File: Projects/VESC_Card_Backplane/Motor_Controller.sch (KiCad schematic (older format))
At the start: 0 parts

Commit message: Added stuff to VESC_Card_Backplane
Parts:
- added P?: AMP17614426-2_EDGE, symbol AMP17614426-2_EDGE
- added P?: EC90_Flat, symbol EC90_Flat
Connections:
- new net W: P?.1 (W), P?.7 (P7)
- no-connect marks 0 -> 1
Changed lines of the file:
@@
 $Descr A4 11693 8268
 encoding utf-8
-Sheet 1 5
+Sheet 3 5
 Title ""
 Date ""
@@
 Comment4 ""
 $EndDescr
+$Comp
+L AMP17614426-2_EDGE P?
+U 1 1 5871B697
+P 5025 3325
+F 0 "P?" H 5025 3775 60  0000 C CNN
+F 1 "AMP17614426-2_EDGE" H 5075 1875 60  0000 C CNN
+F 2 "" H 5175 3325 60  0000 C CNN
+F 3 "" H 5175 3325 60  0000 C CNN
+	1    5025 3325
+	1    0    0    -1
+$EndComp
+NoConn ~ 4525 4575
+$Comp
+L EC90_Flat P?
+U 1 1 5871BA09
+P 3325 4325
+F 0 "P?" H 3325 4575 50  0000 C CNN
+F 1 "EC90_Flat" H 3325 4075 50  0000 C CNN
+F 2 "" H 3325 3125 50  0000 C CNN
+F 3 "" H 3325 3125 50  0000 C CNN
+	1    3325 4325
+	1    0    0    -1
+$EndComp
+Text Label 4525 3075 0    60   ~ 0
+W
+Text Label 3575 4375 0    60   ~ 0
+W
 $EndSCHEMATC

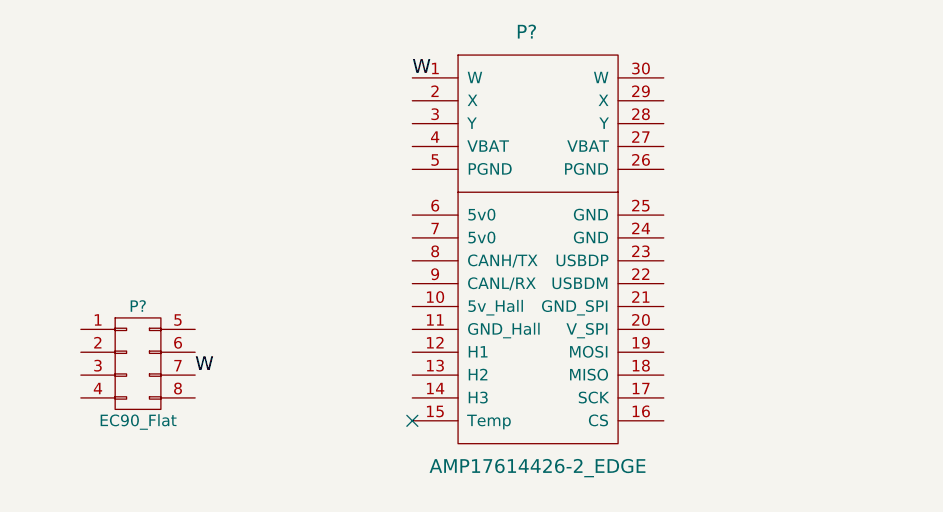
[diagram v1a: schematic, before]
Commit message: Partially did motorcontroller part of schematic
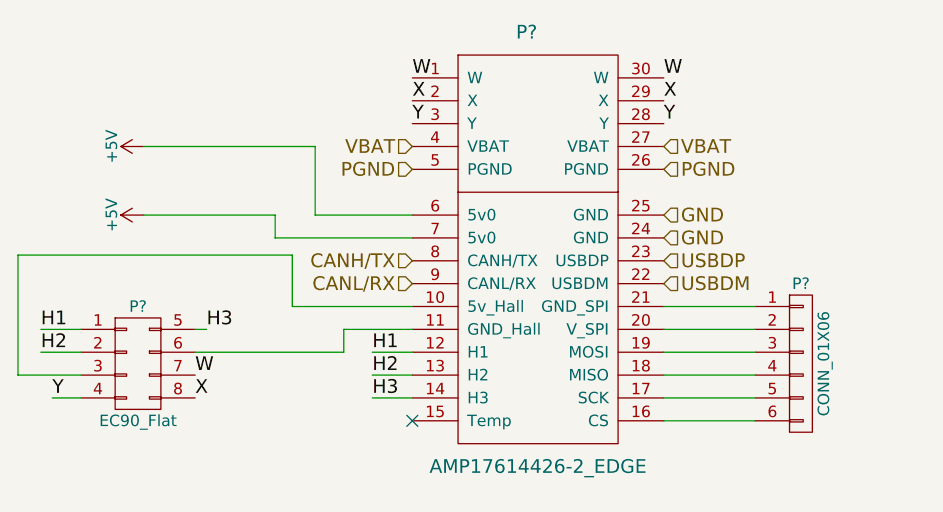
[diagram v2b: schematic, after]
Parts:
- added P?: CONN_01X06, symbol CONN_01X06
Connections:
- net W: now also P?.30 (W)
- net at P?.10 (5v_Hall): now also P?.3 (P3)
- net at P?.11 (GND_Hall): now also P?.6 (P6)
- net H1: now reaches P?.12 (H1)
- net H1: now also P?.1 (P1)
- net H2: now reaches P?.13 (H2)
- net H2: now also P?.2 (P2)
- net H3: now reaches P?.14 (H3)
- net H3: now also P?.5 (P5)
- net at P?.16 (CS): now also P?.6 (P6)
- net at P?.17 (SCK): now also P?.5 (P5)
- net at P?.18 (MISO): now also P?.4 (P4)
- net at P?.19 (MOSI): now also P?.3 (P3)
- net X: now reaches P?.2 (X)
- net X: now also P?.29 (X), P?.8 (P8)
- net at P?.20 (V_SPI): now also P?.2 (P2)
- net at P?.21 (GND_SPI): now also P?.1 (P1)
- net USBDM: now reaches P?.22 (USBDM)
- net USBDP: now reaches P?.23 (USBDP)
- net GND: now reaches P?.24 (GND)
- net GND: now also P?.25 (GND)
- net PGND: now reaches P?.26 (PGND)
- net PGND: now also P?.5 (PGND)
- net VBAT: now reaches P?.27 (VBAT)
- net VBAT: now also P?.4 (VBAT)
- net Y: now reaches P?.28 (Y)
- net Y: now also P?.3 (Y), P?.4 (P4)
- net +5V: now reaches P?.6 (5v0)
- net +5V: now also P?.7 (5v0)
- net CANH/TX: now reaches P?.8 (CANH/TX)
- net CANL/RX: now reaches P?.9 (CANL/RX)
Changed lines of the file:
@@
 Text Label 3575 4375 0    60   ~ 0
 W
+Text Label 3575 4475 0    60   ~ 0
+X
+Text Label 4525 3175 0    60   ~ 0
+X
+Text Label 4525 3275 0    60   ~ 0
+Y
+Text Label 2950 4475 0    60   ~ 0
+Y
+Text Label 4350 4275 0    60   ~ 0
+H1
+Text Label 4350 4375 0    60   ~ 0
+H2
+Text Label 4350 4475 0    60   ~ 0
+H3
+Text Label 2900 4175 0    60   ~ 0
+H1
+Text Label 2900 4275 0    60   ~ 0
+H2
+Text Label 3625 4175 0    60   ~ 0
+H3
+Text HLabel 4525 3375 0    60   Input ~ 0
+VBAT
+Text HLabel 4525 3475 0    60   Input ~ 0
+PGND
+$Comp
+L +5V #PWR?
+U 1 1 5871CFED
+P 3350 3375
+F 0 "#PWR?" H 3350 3225 50  0001 C CNN
+F 1 "+5V" H 3350 3515 50  0000 C CNN
+F 2 "" H 3350 3375 50  0000 C CNN
+F 3 "" H 3350 3375 50  0000 C CNN
+	1    3350 3375
+	0    -1   -1   0
+$EndComp
+$Comp
+L +5V #PWR?
+U 1 1 5871D005
+P 3350 3675
+F 0 "#PWR?" H 3350 3525 50  0001 C CNN
+F 1 "+5V" H 3350 3815 50  0000 C CNN
+F 2 "" H 3350 3675 50  0000 C CNN
+F 3 "" H 3350 3675 50  0000 C CNN
+	1    3350 3675
+	0    -1   -1   0
+$EndComp
+Text HLabel 4525 3875 0    60   Input ~ 0
+CANH/TX
+Text HLabel 4525 3975 0    60   Input ~ 0
+CANL/RX
+Wire Wire Line
+	4525 4275 4350 4275
+Wire Wire Line
+	4525 4375 4350 4375
+Wire Wire Line
+	4525 4475 4350 4475
+Wire Wire Line
+	3575 4275 4225 4275
+Wire Wire Line
+	4225 4275 4225 4175
+Wire Wire Line
+	4225 4175 4525 4175
+Wire Wire Line
+	3075 4375 2800 4375
+Wire Wire Line
+	2800 4375 2800 3850
+Wire Wire Line
+	2800 3850 4000 3850
+Wire Wire Line
+	4000 3850 4000 4075
+Wire Wire Line
+	4000 4075 4525 4075
+Wire Wire Line
+	2900 4175 3075 4175
+Wire Wire Line
+	2900 4275 3075 4275
+Wire Wire Line
+	2950 4475 3075 4475
+Wire Wire Line
+	3625 4175 3575 4175
+Wire Wire Line
+	3350 3375 4100 3375
+Wire Wire Line
+	3350 3675 3925 3675
+Wire Wire Line
+	3925 3675 3925 3775
+Wire Wire Line
+	3925 3775 4525 3775
+Wire Wire Line
+	4100 3375 4100 3675
+Wire Wire Line
+	4100 3675 4525 3675
+Text HLabel 5625 3875 2    60   Input ~ 0
+USBDP
+Text HLabel 5625 3975 2    60   Input ~ 0
+USBDM
+Text Label 5625 3075 0    60   ~ 0
+W
+Text Label 5625 3175 0    60   ~ 0
+X
+Text Label 5625 3275 0    60   ~ 0
+Y
+Text HLabel 5625 3375 2    60   Input ~ 0
+VBAT
+Text HLabel 5625 3475 2    60   Input ~ 0
+PGND
+Text HLabel 5625 3675 2    60   Input ~ 0
+GND
+Text HLabel 5625 3775 2    60   Input ~ 0
+GND
+$Comp
+L CONN_01X06 P?
+U 1 1 5871D4B0
+P 6225 4325
+F 0 "P?" H 6225 4675 50  0000 C CNN
+F 1 "CONN_01X06" V 6325 4325 50  0000 C CNN
+F 2 "" H 6225 4325 50  0000 C CNN
+F 3 "" H 6225 4325 50  0000 C CNN
+	1    6225 4325
+	1    0    0    -1
+$EndComp
+Wire Wire Line
+	6025 4075 5625 4075
+Wire Wire Line
+	5625 4175 6025 4175
+Wire Wire Line
+	6025 4275 5625 4275
+Wire Wire Line
+	5625 4375 6025 4375
+Wire Wire Line
+	6025 4475 5625 4475
+Wire Wire Line
+	5625 4575 6025 4575
 $EndSCHEMATC

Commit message: Updated subsheets and added CAN bus :)
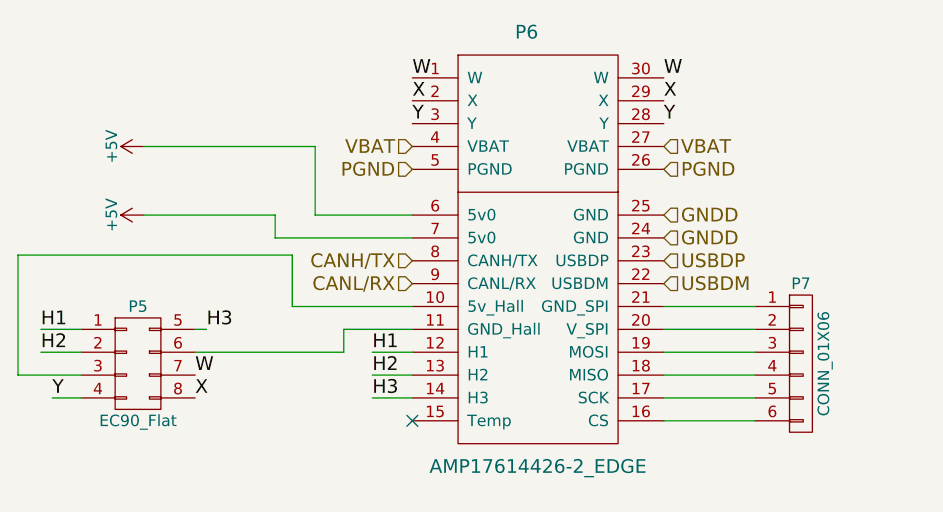
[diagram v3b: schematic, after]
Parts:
- gave numbers to parts that had none: 3
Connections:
- net GND renamed GNDD
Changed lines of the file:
@@
 $Descr A4 11693 8268
 encoding utf-8
-Sheet 3 5
+Sheet 6 6
 Title ""
 Date ""
@@
 $EndDescr
 $Comp
-L AMP17614426-2_EDGE P?
+L AMP17614426-2_EDGE P2
 U 1 1 5871B697
 P 5025 3325
-F 0 "P?" H 5025 3775 60  0000 C CNN
+AR Path="/5871DA4F/5871B697" Ref="P2"  Part="1"
+AR Path="/5878CF59/5871B697" Ref="P6"  Part="1"
+F 0 "P6" H 5025 3775 60  0000 C CNN
 F 1 "AMP17614426-2_EDGE" H 5075 1875 60  0000 C CNN
 F 2 "" H 5175 3325 60  0000 C CNN
@@
 NoConn ~ 4525 4575
 $Comp
-L EC90_Flat P?
+L EC90_Flat P1
 U 1 1 5871BA09
 P 3325 4325
-F 0 "P?" H 3325 4575 50  0000 C CNN
+AR Path="/5871DA4F/5871BA09" Ref="P1"  Part="1"
+AR Path="/5878CF59/5871BA09" Ref="P5"  Part="1"
+F 0 "P5" H 3325 4575 50  0000 C CNN
 F 1 "EC90_Flat" H 3325 4075 50  0000 C CNN
 F 2 "" H 3325 3125 50  0000 C CNN
@@
 PGND
 $Comp
-L +5V #PWR?
+L +5V #PWR4
 U 1 1 5871CFED
 P 3350 3375
-F 0 "#PWR?" H 3350 3225 50  0001 C CNN
+AR Path="/5871DA4F/5871CFED" Ref="#PWR4"  Part="1"
+AR Path="/5878CF59/5871CFED" Ref="#PWR10"  Part="1"
+F 0 "#PWR10" H 3350 3225 50  0001 C CNN
 F 1 "+5V" H 3350 3515 50  0000 C CNN
 F 2 "" H 3350 3375 50  0000 C CNN
@@
 $EndComp
 $Comp
-L +5V #PWR?
+L +5V #PWR5
 U 1 1 5871D005
 P 3350 3675
-F 0 "#PWR?" H 3350 3525 50  0001 C CNN
+AR Path="/5871DA4F/5871D005" Ref="#PWR5"  Part="1"
+AR Path="/5878CF59/5871D005" Ref="#PWR11"  Part="1"
+F 0 "#PWR11" H 3350 3525 50  0001 C CNN
 F 1 "+5V" H 3350 3815 50  0000 C CNN
 F 2 "" H 3350 3675 50  0000 C CNN
@@
 PGND
 Text HLabel 5625 3675 2    60   Input ~ 0
-GND
+GNDD
 Text HLabel 5625 3775 2    60   Input ~ 0
-GND
+GNDD
 $Comp
-L CONN_01X06 P?
+L CONN_01X06 P3
 U 1 1 5871D4B0
 P 6225 4325
-F 0 "P?" H 6225 4675 50  0000 C CNN
+AR Path="/5871DA4F/5871D4B0" Ref="P3"  Part="1"
+AR Path="/5878CF59/5871D4B0" Ref="P7"  Part="1"
+F 0 "P7" H 6225 4675 50  0000 C CNN
 F 1 "CONN_01X06" V 6325 4325 50  0000 C CNN
 F 2 "" H 6225 4325 50  0000 C CNN

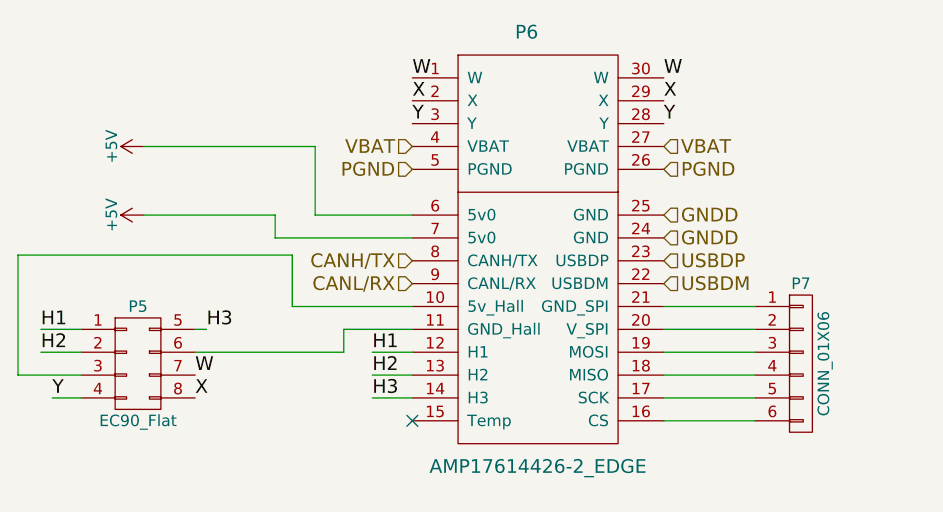
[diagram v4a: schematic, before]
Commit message: Footprint assoc. for backplane
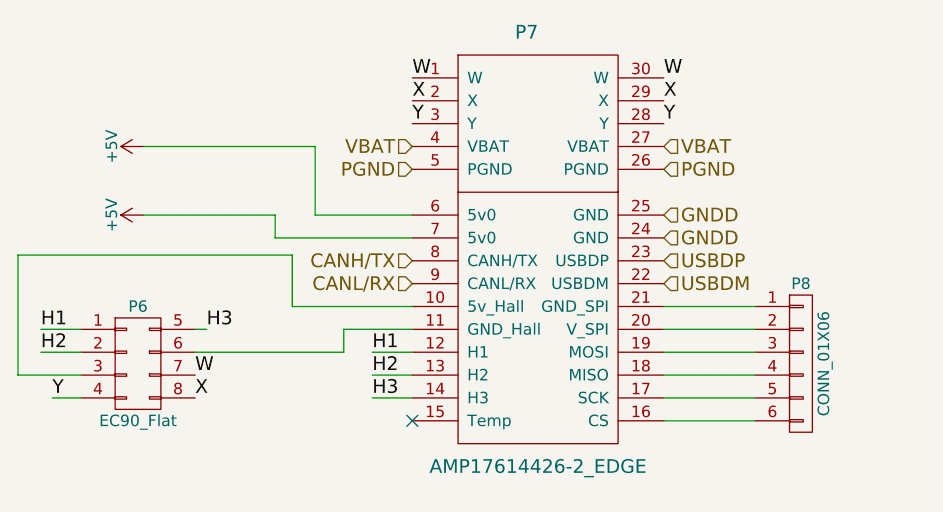
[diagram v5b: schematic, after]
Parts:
- P2: renamed from P1; footprint (none) -> Connectors_Molex:Molex_MiniFit-JR-5569-08A2_2x04x4.20mm_Angled
- P3: renamed from P2; footprint (none) -> USST-footprints:TE2007088-1_Backplane
- P4: renamed from P3; footprint (none) -> USST-footprints:Molex_39502_1006R
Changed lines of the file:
@@
 $Descr A4 11693 8268
 encoding utf-8
-Sheet 6 7
+Sheet 3 7
 Title ""
 Date ""
@@
 $EndDescr
 $Comp
-L AMP17614426-2_EDGE P2
+L AMP17614426-2_EDGE P3
 U 1 1 5871B697
 P 5025 3325
-AR Path="/5871DA4F/5871B697" Ref="P2"  Part="1"
-AR Path="/5878CF59/5871B697" Ref="P6"  Part="1"
-F 0 "P6" H 5025 3775 60  0000 C CNN
+AR Path="/5871DA4F/5871B697" Ref="P3"  Part="1"
+AR Path="/5878CF59/5871B697" Ref="P7"  Part="1"
+AR Path="/5878D5C8/5871B697" Ref="P10"  Part="1"
+F 0 "P7" H 5025 3775 60  0000 C CNN
 F 1 "AMP17614426-2_EDGE" H 5075 1875 60  0000 C CNN
-F 2 "" H 5175 3325 60  0000 C CNN
+F 2 "USST-footprints:TE2007088-1_Backplane" H 5175 3325 60  0001 C CNN
 F 3 "" H 5175 3325 60  0000 C CNN
 	1    5025 3325
@@
 NoConn ~ 4525 4575
 $Comp
-L EC90_Flat P1
+L EC90_Flat P2
 U 1 1 5871BA09
 P 3325 4325
-AR Path="/5871DA4F/5871BA09" Ref="P1"  Part="1"
-AR Path="/5878CF59/5871BA09" Ref="P5"  Part="1"
-F 0 "P5" H 3325 4575 50  0000 C CNN
+AR Path="/5871DA4F/5871BA09" Ref="P2"  Part="1"
+AR Path="/5878CF59/5871BA09" Ref="P6"  Part="1"
+AR Path="/5878D5C8/5871BA09" Ref="P9"  Part="1"
+F 0 "P6" H 3325 4575 50  0000 C CNN
 F 1 "EC90_Flat" H 3325 4075 50  0000 C CNN
-F 2 "" H 3325 3125 50  0000 C CNN
+F 2 "Connectors_Molex:Molex_MiniFit-JR-5569-08A2_2x04x4.20mm_Angled" H 3325 3125 50  0001 C CNN
 F 3 "" H 3325 3125 50  0000 C CNN
 	1    3325 4325
@@
 PGND
 $Comp
-L +5V #PWR4
+L +5V #PWR010
 U 1 1 5871CFED
 P 3350 3375
-AR Path="/5871DA4F/5871CFED" Ref="#PWR4"  Part="1"
-AR Path="/5878CF59/5871CFED" Ref="#PWR10"  Part="1"
-F 0 "#PWR10" H 3350 3225 50  0001 C CNN
+AR Path="/5871DA4F/5871CFED" Ref="#PWR010"  Part="1"
+AR Path="/5878CF59/5871CFED" Ref="#PWR016"  Part="1"
+AR Path="/5878D5C8/5871CFED" Ref="#PWR018"  Part="1"
+F 0 "#PWR018" H 3350 3225 50  0001 C CNN
 F 1 "+5V" H 3350 3515 50  0000 C CNN
 F 2 "" H 3350 3375 50  0000 C CNN
@@
 $EndComp
 $Comp
-L +5V #PWR5
+L +5V #PWR011
 U 1 1 5871D005
 P 3350 3675
-AR Path="/5871DA4F/5871D005" Ref="#PWR5"  Part="1"
-AR Path="/5878CF59/5871D005" Ref="#PWR11"  Part="1"
-F 0 "#PWR11" H 3350 3525 50  0001 C CNN
+AR Path="/5871DA4F/5871D005" Ref="#PWR011"  Part="1"
+AR Path="/5878CF59/5871D005" Ref="#PWR017"  Part="1"
+AR Path="/5878D5C8/5871D005" Ref="#PWR019"  Part="1"
+F 0 "#PWR019" H 3350 3525 50  0001 C CNN
 F 1 "+5V" H 3350 3815 50  0000 C CNN
 F 2 "" H 3350 3675 50  0000 C CNN
@@
 GNDD
 $Comp
-L CONN_01X06 P3
+L CONN_01X06 P4
 U 1 1 5871D4B0
 P 6225 4325
-AR Path="/5871DA4F/5871D4B0" Ref="P3"  Part="1"
-AR Path="/5878CF59/5871D4B0" Ref="P7"  Part="1"
-F 0 "P7" H 6225 4675 50  0000 C CNN
+AR Path="/5871DA4F/5871D4B0" Ref="P4"  Part="1"
+AR Path="/5878CF59/5871D4B0" Ref="P8"  Part="1"
+AR Path="/5878D5C8/5871D4B0" Ref="P11"  Part="1"
+F 0 "P8" H 6225 4675 50  0000 C CNN
 F 1 "CONN_01X06" V 6325 4325 50  0000 C CNN
-F 2 "" H 6225 4325 50  0000 C CNN
+F 2 "USST-footprints:Molex_39502_1006R" H 6225 4325 50  0001 C CNN
 F 3 "" H 6225 4325 50  0000 C CNN
 	1    6225 4325

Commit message: Connected DP's and DM's
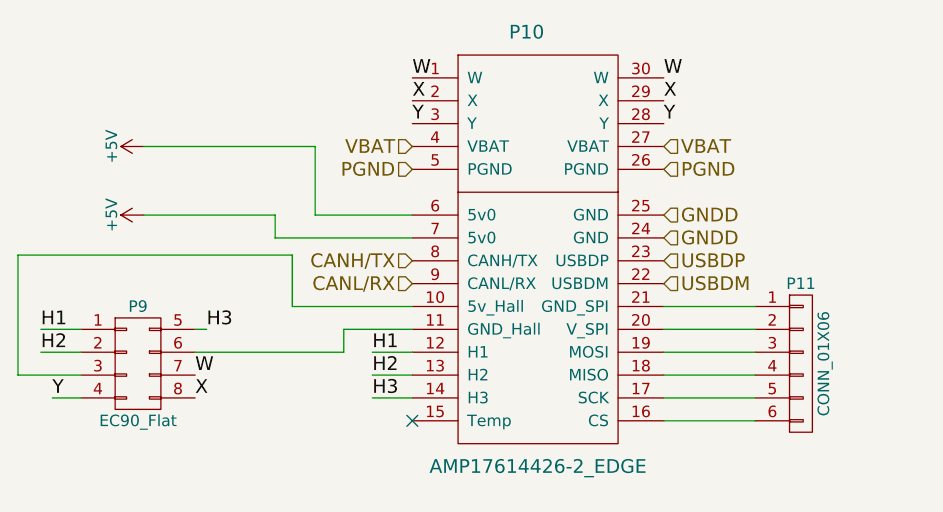
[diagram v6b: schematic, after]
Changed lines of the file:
@@
 AR Path="/5878CF59/5871B697" Ref="P7"  Part="1"
 AR Path="/5878D5C8/5871B697" Ref="P10"  Part="1"
-F 0 "P7" H 5025 3775 60  0000 C CNN
+F 0 "P10" H 5025 3775 60  0000 C CNN
 F 1 "AMP17614426-2_EDGE" H 5075 1875 60  0000 C CNN
 F 2 "USST-footprints:TE2007088-1_Backplane" H 5175 3325 60  0001 C CNN
@@
 AR Path="/5878CF59/5871BA09" Ref="P6"  Part="1"
 AR Path="/5878D5C8/5871BA09" Ref="P9"  Part="1"
-F 0 "P6" H 3325 4575 50  0000 C CNN
+F 0 "P9" H 3325 4575 50  0000 C CNN
 F 1 "EC90_Flat" H 3325 4075 50  0000 C CNN
 F 2 "Connectors_Molex:Molex_MiniFit-JR-5569-08A2_2x04x4.20mm_Angled" H 3325 3125 50  0001 C CNN
@@
 AR Path="/5878CF59/5871D4B0" Ref="P8"  Part="1"
 AR Path="/5878D5C8/5871D4B0" Ref="P11"  Part="1"
-F 0 "P8" H 6225 4675 50  0000 C CNN
+F 0 "P11" H 6225 4675 50  0000 C CNN
 F 1 "CONN_01X06" V 6325 4325 50  0000 C CNN
 F 2 "USST-footprints:Molex_39502_1006R" H 6225 4325 50  0001 C CNN

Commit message: Comleted VESC Backplane
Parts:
- added P12: CONN_01X02, Pin_Headers:Pin_Header_Straight_2x01_Pitch1.27mm, symbol CONN_01X02
- P4: footprint USST-footprints:Molex_39502_1006R -> Pin_Headers:Pin_Header_Angled_2x03_Pitch2.54mm
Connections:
- net at P3.15 (Temp): now also P12.2 (P2)
- net at P3.16 (CS): now also P4.2 (P2); no longer P4.6 (P6)
- net at P3.17 (SCK): now also P4.1 (P1); no longer P4.5 (P5)
- net at P3.20 (V_SPI): now also P4.5 (P5); no longer P4.2 (P2)
- net GND_AUX: now reaches P3.21 (GND_SPI)
- net GND_AUX: now also P4.6 (P6), P12.1 (P1); no longer P4.1 (P1)
- no-connect marks 1 -> 0
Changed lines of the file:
@@
 	1    0    0    -1
 $EndComp
-NoConn ~ 4525 4575
 $Comp
 L EC90_Flat P2
@@
 PGND
 $Comp
-L +5V #PWR010
+L +5V #PWR07
 U 1 1 5871CFED
 P 3350 3375
-AR Path="/5871DA4F/5871CFED" Ref="#PWR010"  Part="1"
-AR Path="/5878CF59/5871CFED" Ref="#PWR016"  Part="1"
-AR Path="/5878D5C8/5871CFED" Ref="#PWR018"  Part="1"
-F 0 "#PWR018" H 3350 3225 50  0001 C CNN
+AR Path="/5871DA4F/5871CFED" Ref="#PWR07"  Part="1"
+AR Path="/5878CF59/5871CFED" Ref="#PWR013"  Part="1"
+AR Path="/5878D5C8/5871CFED" Ref="#PWR015"  Part="1"
+F 0 "#PWR015" H 3350 3225 50  0001 C CNN
 F 1 "+5V" H 3350 3515 50  0000 C CNN
 F 2 "" H 3350 3375 50  0000 C CNN
@@
 $EndComp
 $Comp
-L +5V #PWR011
+L +5V #PWR08
 U 1 1 5871D005
 P 3350 3675
-AR Path="/5871DA4F/5871D005" Ref="#PWR011"  Part="1"
-AR Path="/5878CF59/5871D005" Ref="#PWR017"  Part="1"
-AR Path="/5878D5C8/5871D005" Ref="#PWR019"  Part="1"
-F 0 "#PWR019" H 3350 3525 50  0001 C CNN
+AR Path="/5871DA4F/5871D005" Ref="#PWR08"  Part="1"
+AR Path="/5878CF59/5871D005" Ref="#PWR014"  Part="1"
+AR Path="/5878D5C8/5871D005" Ref="#PWR016"  Part="1"
+F 0 "#PWR016" H 3350 3525 50  0001 C CNN
 F 1 "+5V" H 3350 3815 50  0000 C CNN
 F 2 "" H 3350 3675 50  0000 C CNN
@@
 Text HLabel 4525 3975 0    60   Input ~ 0
 CANL/RX
-Wire Wire Line
-	4525 4275 4350 4275
-Wire Wire Line
-	4525 4375 4350 4375
-Wire Wire Line
-	4525 4475 4350 4475
-Wire Wire Line
-	3575 4275 4225 4275
-Wire Wire Line
-	4225 4275 4225 4175
-Wire Wire Line
-	4225 4175 4525 4175
-Wire Wire Line
-	3075 4375 2800 4375
-Wire Wire Line
-	2800 4375 2800 3850
-Wire Wire Line
-	2800 3850 4000 3850
-Wire Wire Line
-	4000 3850 4000 4075
-Wire Wire Line
-	4000 4075 4525 4075
-Wire Wire Line
-	2900 4175 3075 4175
-Wire Wire Line
-	2900 4275 3075 4275
-Wire Wire Line
-	2950 4475 3075 4475
-Wire Wire Line
-	3625 4175 3575 4175
-Wire Wire Line
-	3350 3375 4100 3375
-Wire Wire Line
-	3350 3675 3925 3675
-Wire Wire Line
-	3925 3675 3925 3775
-Wire Wire Line
-	3925 3775 4525 3775
-Wire Wire Line
-	4100 3375 4100 3675
-Wire Wire Line
-	4100 3675 4525 3675
 Text HLabel 5625 3875 2    60   Input ~ 0
 USBDP
@@
 F 0 "P11" H 6225 4675 50  0000 C CNN
 F 1 "CONN_01X06" V 6325 4325 50  0000 C CNN
-F 2 "USST-footprints:Molex_39502_1006R" H 6225 4325 50  0001 C CNN
+F 2 "Pin_Headers:Pin_Header_Angled_2x03_Pitch2.54mm" H 6225 4325 50  0001 C CNN
 F 3 "" H 6225 4325 50  0000 C CNN
 	1    6225 4325
@@
 $EndComp
 Wire Wire Line
-	6025 4075 5625 4075
-Wire Wire Line
-	5625 4175 6025 4175
+	4525 4275 4350 4275
+Wire Wire Line
+	4525 4375 4350 4375
+Wire Wire Line
+	4525 4475 4350 4475
+Wire Wire Line
+	3575 4275 4225 4275
+Wire Wire Line
+	4225 4275 4225 4175
+Wire Wire Line
+	4225 4175 4525 4175
+Wire Wire Line
+	3075 4375 2800 4375
+Wire Wire Line
+	2800 4375 2800 3850
+Wire Wire Line
+	2800 3850 4000 3850
+Wire Wire Line
+	4000 3850 4000 4075
+Wire Wire Line
+	4000 4075 4525 4075
+Wire Wire Line
+	2900 4175 3075 4175
+Wire Wire Line
+	2900 4275 3075 4275
+Wire Wire Line
+	2950 4475 3075 4475
+Wire Wire Line
+	3625 4175 3575 4175
+Wire Wire Line
+	3350 3375 4100 3375
+Wire Wire Line
+	3350 3675 3925 3675
+Wire Wire Line
+	3925 3675 3925 3775
+Wire Wire Line
+	3925 3775 4525 3775
+Wire Wire Line
+	4100 3375 4100 3675
+Wire Wire Line
+	4100 3675 4525 3675
 Wire Wire Line
 	6025 4275 5625 4275
@@
 	5625 4375 6025 4375
 Wire Wire Line
-	6025 4475 5625 4475
-Wire Wire Line
-	5625 4575 6025 4575
+	5625 4475 5725 4475
+Wire Wire Line
+	5725 4475 5725 4075
+Wire Wire Line
+	5725 4075 6025 4075
+Wire Wire Line
+	5625 4075 5675 4075
+Wire Wire Line
+	5675 4075 5675 4125
+Wire Wire Line
+	5675 4125 6000 4125
+Wire Wire Line
+	5900 4125 5900 4575
+Wire Wire Line
+	5625 4575 5800 4575
+Wire Wire Line
+	5800 4575 5800 4175
+Wire Wire Line
+	5800 4175 6025 4175
+Wire Wire Line
+	5625 4175 5675 4175
+Wire Wire Line
+	5675 4175 5675 4225
+Wire Wire Line
+	5675 4225 5850 4225
+Wire Wire Line
+	5900 4575 6025 4575
+Wire Wire Line
+	5850 4225 5850 4475
+Wire Wire Line
+	5850 4475 6025 4475
+$Comp
+L CONN_01X02 P12
+U 1 1 588448BA
+P 4125 4625
+AR Path="/5871DA4F/588448BA" Ref="P12"  Part="1"
+AR Path="/5878CF59/588448BA" Ref="P13"  Part="1"
+AR Path="/5878D5C8/588448BA" Ref="P14"  Part="1"
+F 0 "P14" H 4125 4775 50  0000 C CNN
+F 1 "CONN_01X02" V 4225 4625 50  0000 C CNN
+F 2 "Pin_Headers:Pin_Header_Straight_2x01_Pitch1.27mm" H 4125 4625 50  0001 C CNN
+F 3 "" H 4125 4625 50  0000 C CNN
+	1    4125 4625
+	-1   0    0    1
+$EndComp
+Wire Wire Line
+	4325 4575 4525 4575
+Wire Wire Line
+	6000 4125 6000 3800
+Wire Wire Line
+	6000 3800 6300 3800
+Connection ~ 5900 4125
+Text Label 6300 3800 0    60   ~ 0
+GND_AUX
+Text Label 4325 4675 0    60   ~ 0
+GND_AUX
 $EndSCHEMATC
